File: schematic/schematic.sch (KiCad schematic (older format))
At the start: 27 parts, among them J1 BARREL_JACK, J2 CONN_01X17, Q1 BD681, Q10 BD681, Q11 BD681, Q12 BD681, Q13 BD681, Q14 BD681, Q15 BD681, Q16 BD681, Q2 BD681, Q3 BD681, Q4 BD681, Q5 BD681, Q6 BD681, Q7 BD681, Q8 BD681, Q9 BD681, SW1 SW_Push_Dual, SW2 SW_Push_Dual

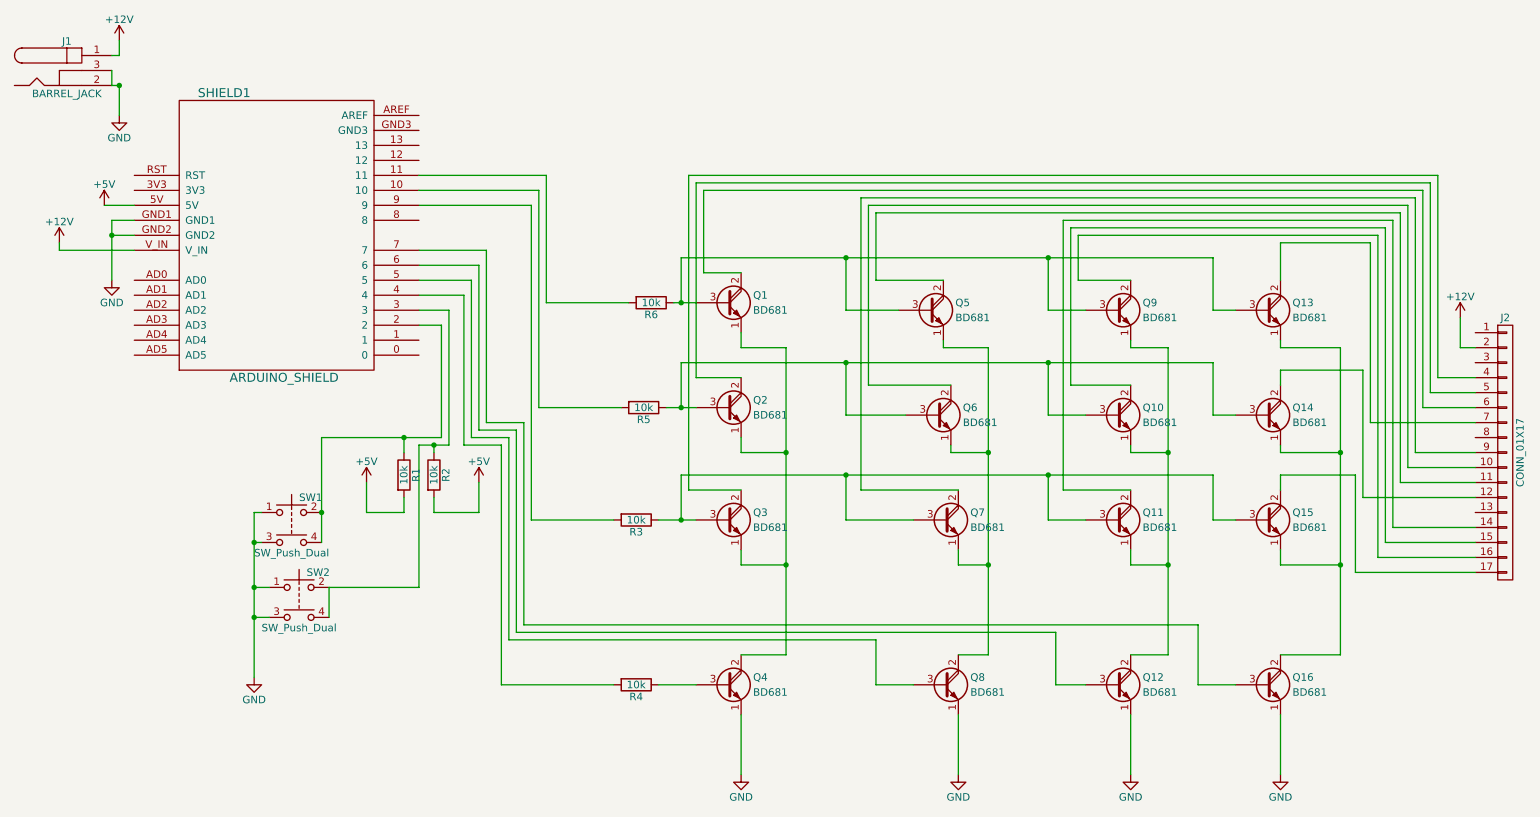
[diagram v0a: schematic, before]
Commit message: pcb v2 - added resistors, changed connectors, changed tracks
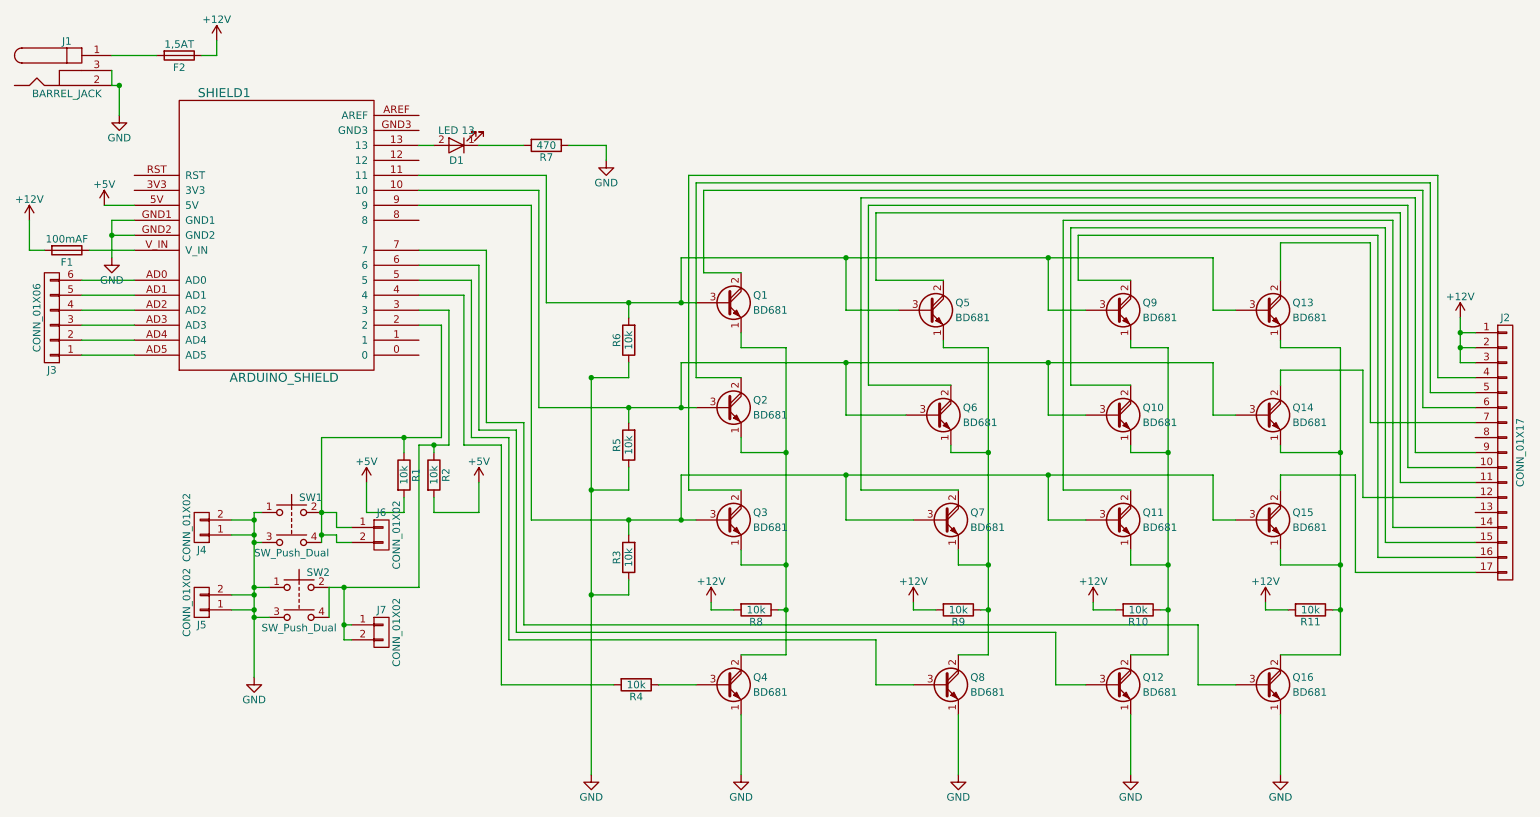
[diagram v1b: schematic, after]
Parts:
- added D1: LED 13, LEDs:LED_0805_HandSoldering, symbol LED
- added F1: 100mAF, Fuse_Holders_and_Fuses:Fuse_SMD1206_Wave, symbol Fuse
- added F2: 1,5AT, Fuse_Holders_and_Fuses:Fuse_SMD1206_Wave, symbol Fuse
- added J3: CONN_01X06, Pin_Headers:Pin_Header_Straight_1x06_Pitch2.54mm, symbol CONN_01X06
- added J4, J5, J6, J7: CONN_01X02, Pin_Headers:Pin_Header_Straight_1x02_Pitch2.54mm, symbol CONN_01X02
- added R10, R11, R8, R9: 10k, Resistors_SMD:R_0805_HandSoldering, symbol R
- added R7: 470, Resistors_SMD:R_0805_HandSoldering, symbol R
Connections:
- net +12V: now also J2.1 (P1), J2.3 (P3), F1.2, F2.1, R10.2, R11.2, R8.2, R9.2; no longer J1.1, SHIELD1.V_IN
- net GND: now also R3.1, R5.1, R6.1, J4.1 (P1), J4.2 (P2), J5.1 (P1), J5.2 (P2), R7.1
- net at R5.2, SHIELD1.10: now also Q10.3 (B), Q14.3 (B), Q2.3 (B), Q6.3 (B)
- net at R6.2, SHIELD1.11: now also Q1.3 (B), Q13.3 (B), Q5.3 (B), Q9.3 (B)
- net at SHIELD1.13: now also D1.2 (A)
- net at R1.1, SHIELD1.2, SW1.2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: now also J6.1 (P1), J6.2 (P2)
- net at R2.1, SHIELD1.3, SW2.2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: now also J7.1 (P1), J7.2 (P2)
- net at R3.2, SHIELD1.9: now also Q11.3 (B), Q15.3 (B), Q3.3 (B), Q7.3 (B)
- net at SHIELD1.AD0: now also J3.6 (P6)
- net at SHIELD1.AD1: now also J3.5 (P5)
- net at SHIELD1.AD2: now also J3.4 (P4)
- net at SHIELD1.AD3: now also J3.3 (P3)
- net at SHIELD1.AD4: now also J3.2 (P2)
- net at SHIELD1.AD5: now also J3.1 (P1)
- net at Q1.1 (E), Q2.1 (E), Q3.1 (E)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: now also R8.1
- net at Q5.1 (E), Q6.1 (E), Q7.1 (E)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: now also R9.1
- net at Q10.1 (E), Q11.1 (E), Q12.2 (C)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: now also R10.1
- net at Q13.1 (E), Q14.1 (E), Q15.1 (E)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: now also R11.1
- new net: F1.1, SHIELD1.V_IN
- new net: F2.2, J1.1
- new net: D1.1 (K), R7.2
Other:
- moved on the sheet: R3, R5, R6
